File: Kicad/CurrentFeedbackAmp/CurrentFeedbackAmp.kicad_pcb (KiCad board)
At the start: 2 copper layers, 86.4 x 55.9 mm, 86 parts, among them J1 Conn_01x01, J10 Conn_01x01, J11 Conn_01x01, J12 Conn_01x01, J13 Conn_01x01, J14 Conn_01x01, J2 Conn_01x01, J3 Conn_01x01, J4 Conn_01x01, J5 Conn_01x01, J6 Conn_01x01, J7 Conn_01x01, J8 Conn_01x01, J9 Conn_01x01, Q1 TIP42C, Q13 BC559, Q14 BC559, Q15 BC559, Q16 BC549, Q17 BC549, Q18 BC549, Q19 BC559, Q20 BC549, Q21 BC559, Q22 BC549, Q24 BD136, Q33 BD135, Q34 TIP41C, Q35 BC559, Q36 BC549, Q37 BC549, Q38 BC549, Q39 BC549, Q40 BC559, Q41 BC559, Q42 BC559, T1 BC548, T2 BC548, U2 TL082

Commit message: Agregué el borde de la placa
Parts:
- moved Q39 91.4 mm to (-19.0, 157.6)
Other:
- board size 86.4 x 55.9 mm -> 200 x 100 mm
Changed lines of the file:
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@@
     (links 138)
     (no_connects 137)
-    (area 0 0 0 0)
+    (area -269.275001 36.695 138.505001 182.795)
     (thickness 1.6)
-    (drawings 22)
+    (drawings 4)
     (tracks 3)
     (zones 0)
@@
   )
   (module TO_SOT_Packages_THT:TO-92_Inline_Narrow_Oval (layer F.Cu)
-    (at 72.39 157.48)
+    (at -18.9865 157.607)
     (descr "TO-92 leads in-line, narrow, oval pads, drill 0.6mm (see NXP sot054_po.pdf)")
     (tags "to-92 sc-43 sc-43a sot54 PA33 transistor")
@@
     )
   )
-  (gr_line (start 54.61 105.41) (end 52.07 107.95) (angle 90) (layer Edge.Cuts) (width 0.15))
-  (gr_line (start 138.43 105.41) (end 54.61 105.41) (angle 90) (layer Edge.Cuts) (width 0.15))
-  (gr_line (start 138.43 161.29) (end 138.43 105.41) (angle 90) (layer Edge.Cuts) (width 0.15))
-  (gr_line (start 52.07 161.29) (end 138.43 161.29) (angle 90) (layer Edge.Cuts) (width 0.15))
-  (gr_line (start 52.07 107.95) (end 52.07 161.29) (angle 90) (layer Edge.Cuts) (width 0.15))
-  (gr_line (start 102.87 55.88) (end 101.6 55.88) (angle 90) (layer Margin) (width 0.2))
-  (gr_line (start 106.68 52.07) (end 102.87 55.88) (angle 90) (layer Margin) (width 0.2))
-  (gr_line (start 101.6 57.15) (end 106.68 52.07) (angle 90) (layer Margin) (width 0.2))
-  (gr_line (start 120.65 57.15) (end 101.6 57.15) (angle 90) (layer Margin) (width 0.2))
-  (gr_line (start 147.32 83.82) (end 120.65 57.15) (angle 90) (layer Margin) (width 0.2))
-  (gr_line (start 224.79 63.5) (end 196.85 91.44) (angle 90) (layer Margin) (width 0.2))
-  (gr_line (start 199.39 63.5) (end 224.79 63.5) (angle 90) (layer Margin) (width 0.2))
-  (gr_line (start 100.33 55.88) (end 149.86 55.88) (angle 90) (layer Margin) (width 0.2))
-  (gr_line (start 242.57 109.22) (end 224.79 109.22) (angle 90) (layer Margin) (width 0.2))
-  (gr_line (start 242.57 40.64) (end 242.57 109.22) (angle 90) (layer Margin) (width 0.2))
-  (gr_line (start 45.72 19.05) (end 240.03 19.05) (angle 90) (layer Margin) (width 0.2))
-  (gr_line (start 46.99 17.78) (end 45.72 19.05) (angle 90) (layer Margin) (width 0.2))
-  (gr_line (start 46.99 12.7) (end 46.99 17.78) (angle 90) (layer Margin) (width 0.2))
-  (gr_line (start 219.71 12.7) (end 46.99 12.7) (angle 90) (layer Margin) (width 0.2))
-  (gr_line (start 222.25 116.84) (end 222.25 34.29) (angle 90) (layer Margin) (width 0.2))
-  (gr_line (start 45.72 95.25) (end 219.71 95.25) (angle 90) (layer Margin) (width 0.2))
-  (gr_line (start 45.72 19.05) (end 45.72 95.25) (angle 90) (layer Margin) (width 0.2))
+  (gr_line (start 250 40) (end 250 140) (angle 90) (layer Edge.Cuts) (width 0.15))
+  (gr_line (start 50 40) (end 50 140) (angle 90) (layer Edge.Cuts) (width 0.15))
+  (gr_line (start 50 140) (end 250 140) (angle 90) (layer Edge.Cuts) (width 0.15))
+  (gr_line (start 50 40) (end 250 40) (angle 90) (layer Edge.Cuts) (width 0.15))
   (segment (start -154.94 160.02) (end -154.94 166.37) (width 0.25) (layer F.Cu) (net 24))
   (segment (start -143.51 177.8) (end -135.89 177.8) (width 0.25) (layer F.Cu) (net 24))

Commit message: Alinee los transistores en uno de los extremos del pcb
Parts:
- moved Q22 462.4 mm to (221.8, 136.0)
- moved Q38 438.5 mm to (200.0, 135.5)
- moved T2 436.7 mm to (179.3, 135.6)
- moved Q20 422.8 mm to (206.9, 135.6)
- moved Q18 415.9 mm to (214.0, 136.1)
- moved Q37 415.2 mm to (229.3, 136.0)
- moved Q19 368.1 mm to (127.3, 135.9)
- moved Q34 355.4 mm to (151.0, 135.3), turned to 180 degrees
- moved Q21 349.0 mm to (113.4, 136.0)
- moved Q35 348.3 mm to (120.0, 135.7)
- moved Q17 343.1 mm to (193.6, 135.8)
- moved Q33 319.9 mm to (161.5, 135.4), turned to 180 degrees
- moved T1 297.9 mm to (187.1, 135.6)
- moved Q40 290.0 mm to (59.8, 136.2)
- moved Q24 289.0 mm to (171.8, 135.2), turned to 180 degrees
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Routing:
- net Net-(Q1-Pad1): track 30.1 -> 0.00 mm

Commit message: Ahora el PCB tiene agujeros para montar la placa y modifique el modelo de los pines
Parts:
- added MK1: Mounting_Hole, Mounting_Holes:MountingHole_2.2mm_M2, F.Cu at (246.0, 136.0)
- added MK2: Mounting_Hole, Mounting_Holes:MountingHole_2.2mm_M2, F.Cu at (245.9, 43.5)
- added MK3: Mounting_Hole, Mounting_Holes:MountingHole_2.2mm_M2, F.Cu at (54.5, 43.9)
- added MK4: Mounting_Hole, Mounting_Holes:MountingHole_2.2mm_M2, F.Cu at (53.7, 136.3)
- J1, J10, J11, J12, J13, J14, J2, J3, J4, J5, J6, J7, J8, J9: footprint Connectors:1pin -> Connectors:PINTST
- moved U2 222.8 mm to (95.8, 91.2)
- moved J11 147.7 mm to (68.9, 81.8)
- moved Q24 11.3 mm to (183.0, 135.7)
- moved Q33 11.2 mm to (172.7, 135.8)
- moved Q34 10.4 mm to (161.4, 136.0)
- moved Q1 10.4 mm to (149.9, 136.3)
- moved Q35 9.39 mm to (129.3, 136.7)
- moved Q21 9.16 mm to (122.6, 136.5)
- moved Q19 8.54 mm to (135.8, 136.7)
- moved T2 8.49 mm to (187.8, 136.5)
- moved Q38 7.98 mm to (208.0, 136.3)
- moved Q15 7.90 mm to (114.7, 136.5)
- moved Q16 7.78 mm to (107.9, 136.9)
- moved Q20 7.46 mm to (214.3, 136.3)
- moved T1 7.42 mm to (194.4, 136.5)
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
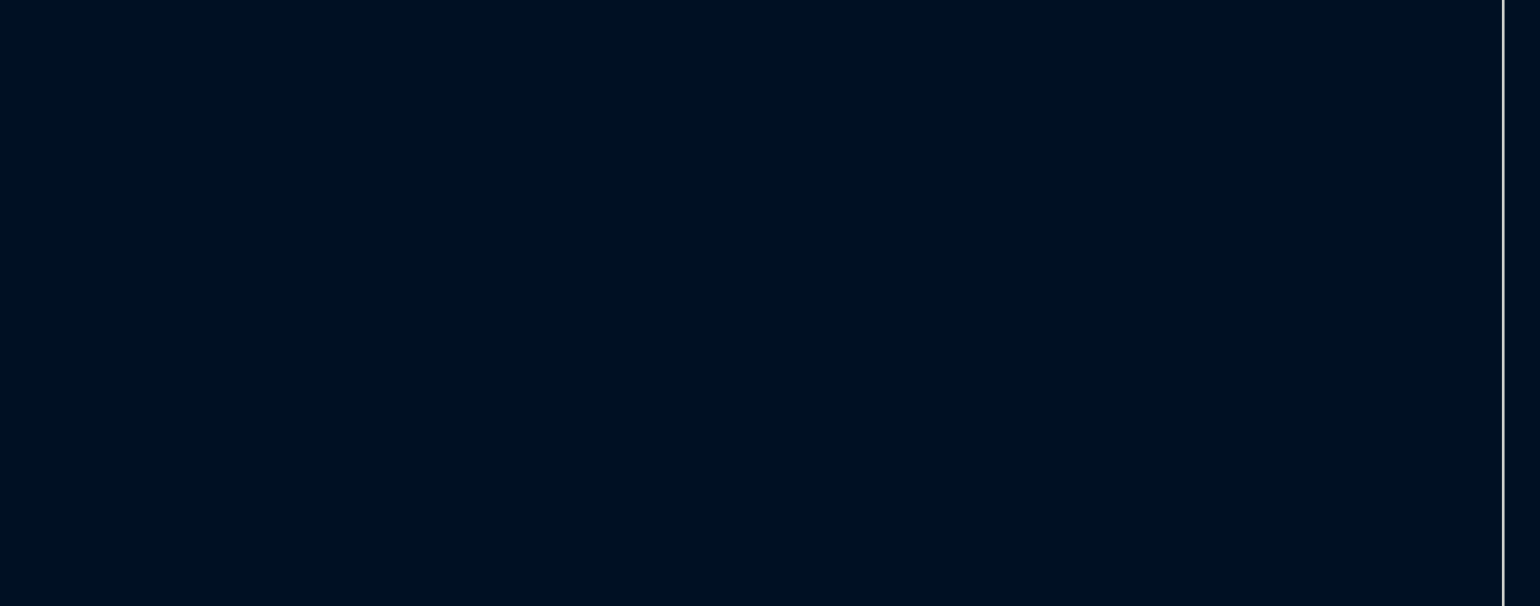
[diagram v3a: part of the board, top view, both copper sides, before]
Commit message: PCB: Bornera, tierras y nombre a los pines
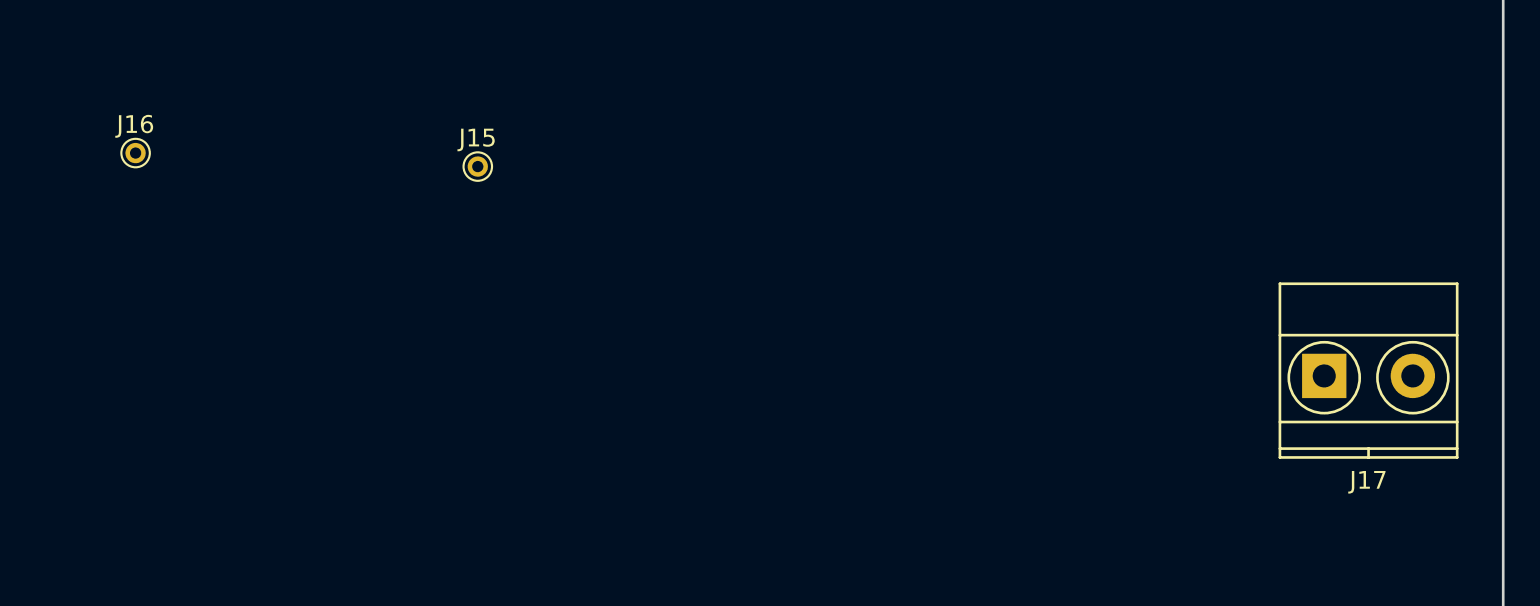
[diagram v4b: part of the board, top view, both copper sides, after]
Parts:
- added J15: Masa Filtros, Connectors:PINTST, F.Cu at (192.2, 93.9)
- added J16: Masa Bornera Carga, Connectors:PINTST, F.Cu at (172.8, 93.1)
- added J17: Bornera Carga, Connectors_Terminal_Blocks:TerminalBlock_Pheonix_MKDS1.5-2pol, F.Cu at (239.9, 105.7)
- J1: value Conn_01x01 -> Vin
- J10: value Conn_01x01 -> Protecc_Sup_In1
- J11: value Conn_01x01 -> Protecc_Inf_In1
- J12: value Conn_01x01 -> Protecc_Sup_In2
- J13: value Conn_01x01 -> Vdd
- J14: value Conn_01x01 -> Vcc
- J2: value Conn_01x01 -> Test_Realim_Out
- J3: value Conn_01x01 -> Masa etapa inicial
- J4: value Conn_01x01 -> Protecc_Sup_Out
- J5: value Conn_01x01 -> Protecc_Inf_Out
- J6: value Conn_01x01 -> VccTL
- J7: value Conn_01x01 -> VddTL
- J8: value Conn_01x01 -> Test_Etapa_3_Inf
- J9: value Conn_01x01 -> Test_Etapa_3_Sup
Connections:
- J3 pad 1: DC.servo.Input -> GND
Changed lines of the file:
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@@
 (kicad_pcb (version 4) (host pcbnew 4.0.7)
   (general
-    (links 138)
-    (no_connects 138)
+    (links 142)
+    (no_connects 142)
     (area 49.924999 39.924999 250.075001 140.075001)
     (thickness 1.6)
@@
     (tracks 0)
     (zones 0)
-    (modules 90)
+    (modules 93)
     (nets 51)
   )
@@
       (effects (font (size 1 1) (thickness 0.15)))
     )
-    (fp_text value Conn_01x01 (at 0 1.6) (layer F.Fab)
+    (fp_text value Vin (at 0 1.6) (layer F.Fab)
       (effects (font (size 1 1) (thickness 0.15)))
     )
@@
       (effects (font (size 1 1) (thickness 0.15)))
     )
-    (fp_text value Conn_01x01 (at 0 1.6) (layer F.Fab)
+    (fp_text value Test_Realim_Out (at 0 1.6) (layer F.Fab)
       (effects (font (size 1 1) (thickness 0.15)))
     )
@@
       (effects (font (size 1 1) (thickness 0.15)))
     )
-    (fp_text value Conn_01x01 (at 0 1.6) (layer F.Fab)
+    (fp_text value "Masa etapa inicial" (at 0 1.6) (layer F.Fab)
       (effects (font (size 1 1) (thickness 0.15)))
     )
@@
     (fp_circle (center 0 0) (end -0.254 -0.762) (layer F.SilkS) (width 0.12))
     (pad 1 thru_hole circle (at 0 0) (size 1.143 1.143) (drill 0.635) (layers *.Cu *.Mask)
-      (net 5 DC.servo.Input))
+      (net 11 GND))
     (model ${KISYS3DMOD}/Connectors.3dshapes/PINTST.wrl
       (at (xyz 0 0 0))
@@
       (effects (font (size 1 1) (thickness 0.15)))
     )
-    (fp_text value Conn_01x01 (at 0 1.6) (layer F.Fab)
+    (fp_text value Protecc_Sup_Out (at 0 1.6) (layer F.Fab)
       (effects (font (size 1 1) (thickness 0.15)))
     )
@@
       (effects (font (size 1 1) (thickness 0.15)))
     )
-    (fp_text value Conn_01x01 (at 0 1.6) (layer F.Fab)
+    (fp_text value Protecc_Inf_Out (at 0 1.6) (layer F.Fab)
       (effects (font (size 1 1) (thickness 0.15)))
     )
@@
       (effects (font (size 1 1) (thickness 0.15)))
     )
-    (fp_text value Conn_01x01 (at 0 1.6) (layer F.Fab)
+    (fp_text value VccTL (at 0 1.6) (layer F.Fab)
       (effects (font (size 1 1) (thickness 0.15)))
     )
@@
       (effects (font (size 1 1) (thickness 0.15)))
     )
-    (fp_text value Conn_01x01 (at 0 1.6) (layer F.Fab)
+    (fp_text value VddTL (at 0 1.6) (layer F.Fab)
       (effects (font (size 1 1) (thickness 0.15)))
     )
@@
       (effects (font (size 1 1) (thickness 0.15)))
     )
-    (fp_text value Conn_01x01 (at 0 1.6) (layer F.Fab)
+    (fp_text value Test_Etapa_3_Inf (at 0 1.6) (layer F.Fab)
       (effects (font (size 1 1) (thickness 0.15)))
     )
@@
       (effects (font (size 1 1) (thickness 0.15)))
     )
-    (fp_text value Conn_01x01 (at 0 1.6) (layer F.Fab)
+    (fp_text value Test_Etapa_3_Sup (at 0 1.6) (layer F.Fab)
       (effects (font (size 1 1) (thickness 0.15)))
     )
@@
       (effects (font (size 1 1) (thickness 0.15)))
     )
-    (fp_text value Conn_01x01 (at 0 1.6) (layer F.Fab)
+    (fp_text value Protecc_Sup_In1 (at 0 1.6) (layer F.Fab)
       (effects (font (size 1 1) (thickness 0.15)))
     )
@@
       (effects (font (size 1 1) (thickness 0.15)))
     )
-    (fp_text value Conn_01x01 (at 0 1.6) (layer F.Fab)
+    (fp_text value Protecc_Inf_In1 (at 0 1.6) (layer F.Fab)
       (effects (font (size 1 1) (thickness 0.15)))
     )
@@
       (effects (font (size 1 1) (thickness 0.15)))
     )
-    (fp_text value Conn_01x01 (at 0 1.6) (layer F.Fab)
+    (fp_text value Protecc_Sup_In2 (at 0 1.6) (layer F.Fab)
       (effects (font (size 1 1) (thickness 0.15)))
     )
@@
       (effects (font (size 1 1) (thickness 0.15)))
     )
-    (fp_text value Conn_01x01 (at 0 1.6) (layer F.Fab)
+    (fp_text value Vdd (at 0 1.6) (layer F.Fab)
       (effects (font (size 1 1) (thickness 0.15)))
     )
@@
       (effects (font (size 1 1) (thickness 0.15)))
     )
-    (fp_text value Conn_01x01 (at 0 1.6) (layer F.Fab)
+    (fp_text value Vcc (at 0 1.6) (layer F.Fab)
       (effects (font (size 1 1) (thickness 0.15)))
     )
@@
       (scale (xyz 1 1 1))
       (rotate (xyz 0 0 0))
+    )
+  )
+  (module Connectors:PINTST (layer F.Cu)
+    (at 192.151 93.853)
+    (descr "module 1 pin (ou trou mecanique de percage)")
+    (tags DEV)
+    (fp_text reference J15 (at 0 -1.6) (layer F.SilkS)
+      (effects (font (size 1 1) (thickness 0.15)))
+    )
+    (fp_text value "Masa Filtros" (at 0 1.6) (layer F.Fab)
+      (effects (font (size 1 1) (thickness 0.15)))
+    )
+    (fp_circle (center 0 0) (end 1.1 0) (layer F.CrtYd) (width 0.05))
+    (fp_circle (center 0 0) (end 0.4 0.6) (layer F.Fab) (width 0.1))
+    (fp_circle (center 0 0) (end -0.254 -0.762) (layer F.SilkS) (width 0.12))
+    (pad 1 thru_hole circle (at 0 0) (size 1.143 1.143) (drill 0.635) (layers *.Cu *.Mask)
+      (net 11 GND))
+    (model ${KISYS3DMOD}/Connectors.3dshapes/PINTST.wrl
+      (at (xyz 0 0 0))
+      (scale (xyz 1 1 1))
+      (rotate (xyz 0 0 0))
+    )
+  )
+  (module Connectors:PINTST (layer F.Cu)
+    (at 172.847 93.091)
+    (descr "module 1 pin (ou trou mecanique de percage)")
+    (tags DEV)
+    (fp_text reference J16 (at 0 -1.6) (layer F.SilkS)
+      (effects (font (size 1 1) (thickness 0.15)))
+    )
+    (fp_text value "Masa Bornera Carga" (at 0 1.6) (layer F.Fab)
+      (effects (font (size 1 1) (thickness 0.15)))
+    )
+    (fp_circle (center 0 0) (end 1.1 0) (layer F.CrtYd) (width 0.05))
+    (fp_circle (center 0 0) (end 0.4 0.6) (layer F.Fab) (width 0.1))
+    (fp_circle (center 0 0) (end -0.254 -0.762) (layer F.SilkS) (width 0.12))
+    (pad 1 thru_hole circle (at 0 0) (size 1.143 1.143) (drill 0.635) (layers *.Cu *.Mask)
+      (net 11 GND))
+    (model ${KISYS3DMOD}/Connectors.3dshapes/PINTST.wrl
+      (at (xyz 0 0 0))
+      (scale (xyz 1 1 1))
+      (rotate (xyz 0 0 0))
+    )
+  )
+  (module Connectors_Terminal_Blocks:TerminalBlock_Pheonix_MKDS1.5-2pol (layer F.Cu)
+    (at 239.903 105.664)
+    (descr "2-way 5mm pitch terminal block, Phoenix MKDS series")
+    (fp_text reference J17 (at 2.5 5.9) (layer F.SilkS)
+      (effects (font (size 1 1) (thickness 0.15)))
+    )
+    (fp_text value "Bornera Carga" (at 2.5 -6.6) (layer F.Fab)
+      (effects (font (size 1 1) (thickness 0.15)))
+    )
+    (fp_line (start -2.7 -5.4) (end 7.7 -5.4) (layer F.CrtYd) (width 0.05))
+    (fp_line (start -2.7 4.8) (end -2.7 -5.4) (layer F.CrtYd) (width 0.05))
+    (fp_line (start 7.7 4.8) (end -2.7 4.8) (layer F.CrtYd) (width 0.05))
+    (fp_line (start 7.7 -5.4) (end 7.7 4.8) (layer F.CrtYd) (width 0.05))
+    (fp_line (start 2.5 4.1) (end 2.5 4.6) (layer F.SilkS) (width 0.15))
+    (fp_circle (center 5 0.1) (end 3 0.1) (layer F.SilkS) (width 0.15))
+    (fp_circle (center 0 0.1) (end 2 0.1) (layer F.SilkS) (width 0.15))
+    (fp_line (start -2.5 2.6) (end 7.5 2.6) (layer F.SilkS) (width 0.15))
+    (fp_line (start -2.5 -2.3) (end 7.5 -2.3) (layer F.SilkS) (width 0.15))
+    (fp_line (start -2.5 4.1) (end 7.5 4.1) (layer F.SilkS) (width 0.15))
+    (fp_line (start -2.5 4.6) (end 7.5 4.6) (layer F.SilkS) (width 0.15))
+    (fp_line (start 7.5 4.6) (end 7.5 -5.2) (layer F.SilkS) (width 0.15))
+    (fp_line (start 7.5 -5.2) (end -2.5 -5.2) (layer F.SilkS) (width 0.15))
+    (fp_line (start -2.5 -5.2) (end -2.5 4.6) (layer F.SilkS) (width 0.15))
+    (pad 1 thru_hole rect (at 0 0) (size 2.5 2.5) (drill 1.3) (layers *.Cu *.Mask)
+      (net 5 DC.servo.Input))
+    (pad 2 thru_hole circle (at 5 0) (size 2.5 2.5) (drill 1.3) (layers *.Cu *.Mask)
+      (net 11 GND))
+    (model Terminal_Blocks.3dshapes/TerminalBlock_Pheonix_MKDS1.5-2pol.wrl
+      (at (xyz 0.0984 0 0))
+      (scale (xyz 1 1 1))
+      (rotate (xyz 0 0 0))

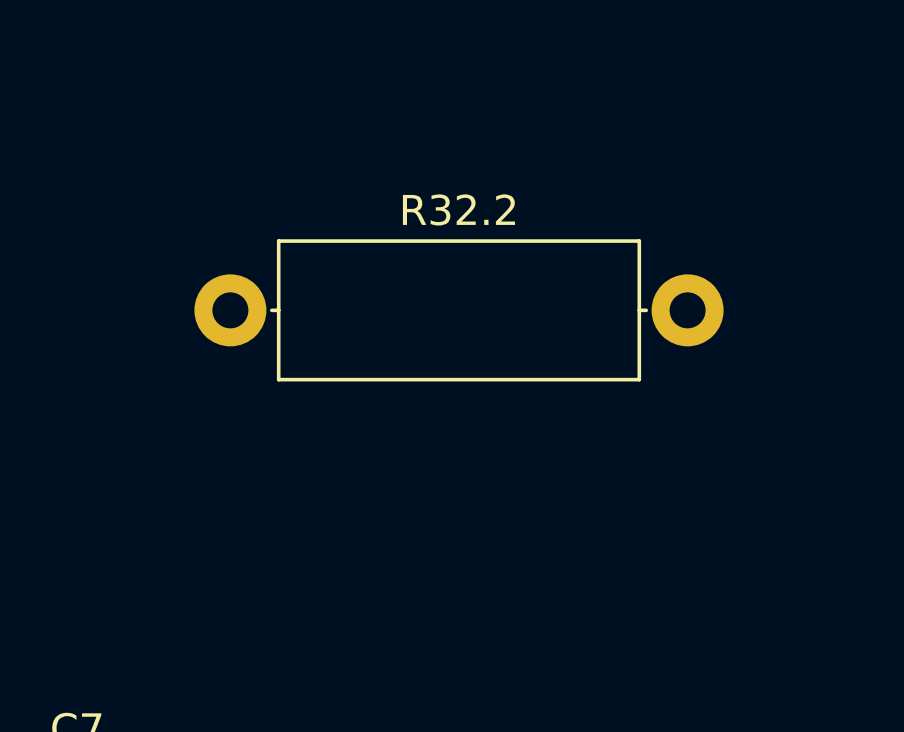
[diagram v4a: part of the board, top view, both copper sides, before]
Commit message: Cambio modelo de capacitores electroliticos
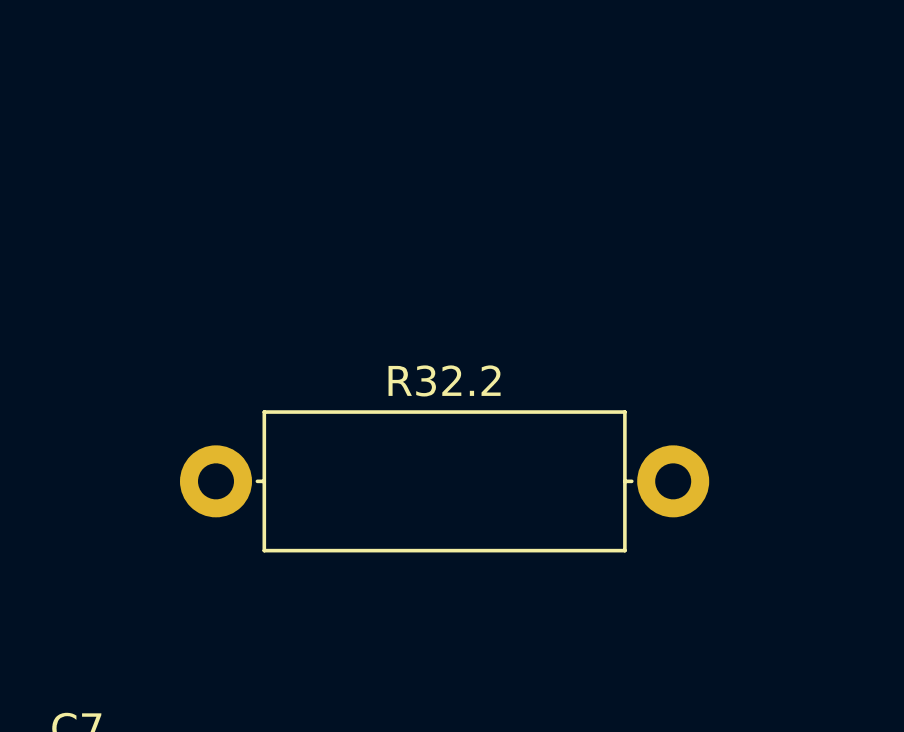
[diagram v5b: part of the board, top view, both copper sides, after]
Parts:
- moved R32.2 5.72 mm to (-135.1, 111.1)
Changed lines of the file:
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@@
   )
   (module Resistors_THT:R_Axial_DIN0414_L11.9mm_D4.5mm_P15.24mm_Horizontal (layer F.Cu)
-    (at -134.62 105.41)
+    (at -135.10006 111.10976)
     (descr "Resistor, Axial_DIN0414 series, Axial, Horizontal, pin pitch=15.24mm, 2W, length*diameter=11.9*4.5mm^2, http://www.vishay.com/docs/20128/wkxwrx.pdf")
     (tags "Resistor Axial_DIN0414 series Axial Horizontal pin pitch 15.24mm 2W length 11.9mm diameter 4.5mm")

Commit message: Configuracion estrella!
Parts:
- moved R20 463.5 mm to (194.3, 129.5), turned to 270 degrees
- moved R16 427.7 mm to (196.8, 129.5), turned to 90 degrees
- moved C1 392.6 mm to (207.0, 94.0)
- moved R31.2 390.0 mm to (224.8, 120.7), turned to 180 degrees
- moved R31.3 388.2 mm to (209.6, 114.3)
- moved R31.1 334.6 mm to (209.6, 127.0)
- moved R32.1 315.0 mm to (90.2, 128.3), turned to 180 degrees
- moved R32.3 306.2 mm to (90.2, 121.9), turned to 180 degrees
- moved Rref3 299.0 mm to (78.7, 61.0)
- moved Rref2 275.2 mm to (171.4, 123.2), turned to 270 degrees
- moved R5 268.0 mm to (184.2, 129.5), turned to 270 degrees
- moved R32.2 225.3 mm to (90.2, 115.6), turned to 180 degrees
- moved R21 224.3 mm to (105.4, 129.5), turned to 270 degrees
- moved Q22 106.0 mm to (121.9, 137.2)
- moved J17 95.8 mm to (148.6, 134.6)
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
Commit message: termindado el acomodo de componentes kicad
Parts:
- moved J14 470.9 mm to (230.5, 72.4)
- moved J7 408.6 mm to (219.1, 75.6)
- moved J6 408.4 mm to (219.1, 81.9)
- moved R18 407.9 mm to (149.8, 105.4)
- moved R19 407.5 mm to (144.1, 75.6)
- moved J4 403.1 mm to (194.3, 81.9)
- moved C8 377.8 mm to (230.5, 94.6), turned to 90 degrees
- moved R30 370.5 mm to (193.0, 66.7)
- moved C3 362.0 mm to (130.8, 106.0)
- moved R6 360.7 mm to (110.5, 74.3)
- moved R17 354.6 mm to (108.0, 128.9), turned to 90 degrees
- moved R11 353.7 mm to (184.7, 74.3)
- moved R15 350.9 mm to (144.1, 69.2), turned to 180 degrees
- moved C5 350.6 mm to (152.4, 69.8)
- moved R10 349.3 mm to (118.1, 128.9), turned to 90 degrees
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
